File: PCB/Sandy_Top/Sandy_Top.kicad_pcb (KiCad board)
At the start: 2 copper layers, 285 x 75.1 mm, 31 parts, among them J2 Conn_02x02_Top_Bottom, J3 Conn_02x02_Top_Bottom

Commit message: 基板外形をLP版に変更。不要ファイル削除。
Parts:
- removed the SW_'1 at (186.6, 65.1)
- REF**: footprint locallib:60_Outline-Sandy-DN0040-Top-sw-hole -> locallib:SandyLP_outline_Top
- moved D17 11.0 mm to (142.5, 44.1), turned to -90 degrees
- moved D19 11.0 mm to (180.6, 44.1), turned to -90 degrees
- moved D16 10.6 mm to (123.5, 44.9), turned to -90 degrees
- moved D18 10.6 mm to (161.6, 44.9), turned to -90 degrees
- moved D15 10.3 mm to (142.5, 64.6), turned to -90 degrees
- moved D20 10.3 mm to (161.6, 64.6), turned to -90 degrees
- moved H10 3.57 mm to (173.5, 55.6)
- moved H9 1.19 mm to (142.5, 55.6)
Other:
- board size 285 x 75.1 mm -> 74.9 x 37 mm

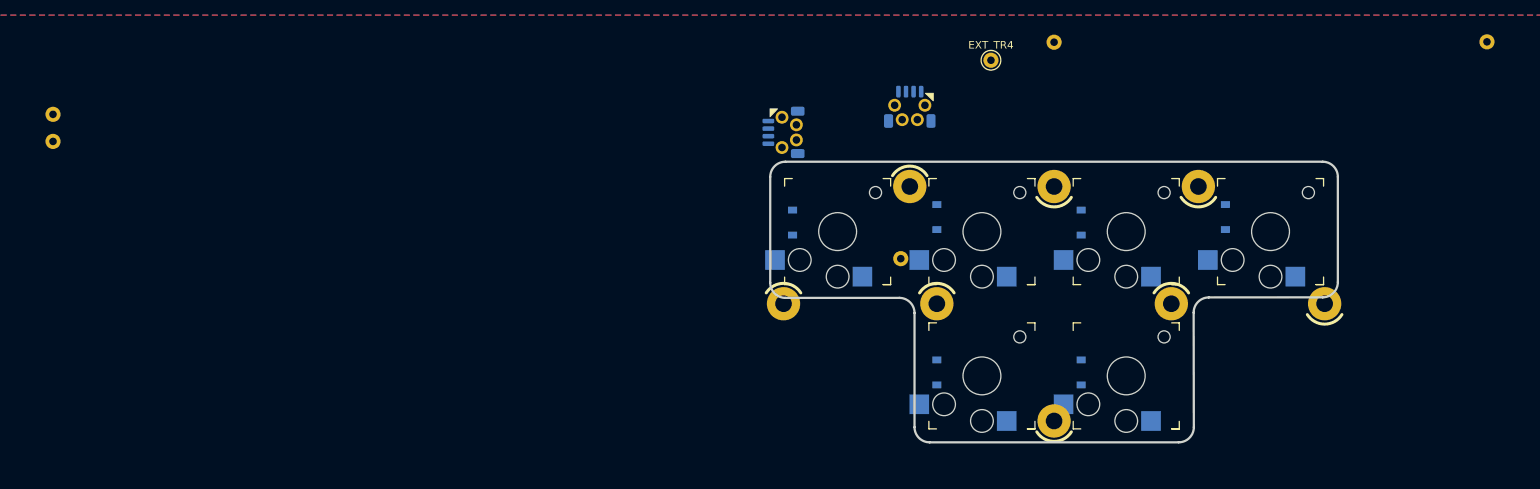
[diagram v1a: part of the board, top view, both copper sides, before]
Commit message: Topを仮配線。Midとの接続も一応確定
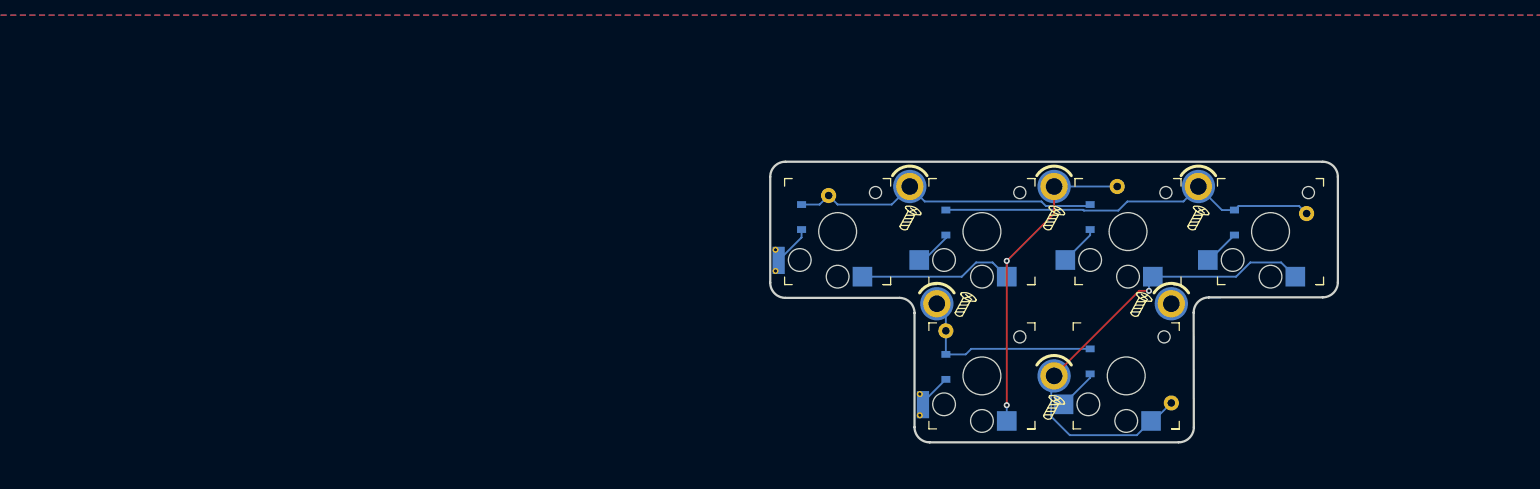
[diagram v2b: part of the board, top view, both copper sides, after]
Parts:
- removed EXT_TR5: Conn_01x01, locallib:TestPoint_THTPad_D2.0mm_Drill1.0mm
- removed the H6 at (177.0, 40.1)
- removed H8: MountingHole, locallib:MountingHole_2.2mm_M2_Pad_minimal
- removed J2, J3: Conn_02x02_Top_Bottom, locallib:JST_SH_SM04B-SRSS-TB_1x04-1MP_P1.00mm_Horizontal_wCable_housing_spare_pin_courtyard
- added REF**: ICON_Screw_Medium, locallib:ICON_Screw_Medium, F.Cu at (157.9, 71.8)
- added REF**: ICON_Screw_Medium, locallib:ICON_Screw_Medium, F.Cu at (169.4, 58.3)
- added REF**: ICON_Screw_Medium, locallib:ICON_Screw_Medium, F.Cu at (138.9, 46.8)
- added REF**: ICON_Screw_Medium, locallib:ICON_Screw_Medium, F.Cu at (157.9, 46.8)
- added REF**: ICON_Screw_Medium, locallib:ICON_Screw_Medium, F.Cu at (176.9, 46.8)
- added REF**: ICON_Screw_Medium, locallib:ICON_Screw_Medium, F.Cu at (146.2, 58.3)
- EXT_TR4: moved to B.Cu
- H1: renamed from H2; footprint locallib:MountingHole_2.2mm_M2_Pad_minimal -> locallib:MountingHole_1.8-2.2mm_M2_Pad_minimal
- H2: renamed from H3; footprint locallib:MountingHole_2.2mm_M2_Pad_minimal -> locallib:MountingHole_1.8-2.2mm_M2_Pad_minimal
- H3: renamed from H11; footprint locallib:MountingHole_2.2mm_M2_Pad_minimal -> locallib:MountingHole_1.8-2.2mm_M2_Pad_minimal
- H4: renamed from H12; footprint locallib:MountingHole_2.2mm_M2_Pad_minimal -> locallib:MountingHole_1.8-2.2mm_M2_Pad_minimal
- H5: renamed from H9; footprint locallib:MountingHole_2.2mm_M2_Pad_minimal -> locallib:MountingHole_1.8-2.2mm_M2_Pad_minimal
- H6: renamed from H10; footprint locallib:MountingHole_2.2mm_M2_Pad_minimal -> locallib:MountingHole_1.8-2.2mm_M2_Pad_minimal
- SW_;1, SW_[1: footprint locallib:Kailh_socket_ChocV2 -> locallib:Kailh_socket_ChocV2_small_#2pad
- moved EXT_TR0 103.0 mm to (128.2, 41.3)
- moved EXT_TC4 63.3 mm to (173.5, 68.7)
- moved D4 58.3 mm to (181.8, 44.9)
- moved SW_T1 57.2 mm to (186.6, 46.1)
- moved H3 56.9 mm to (177.0, 40.1)
- moved EXT_TR4 46.3 mm to (191.3, 43.7), turned to 180 degrees
- moved H2 38.9 mm to (158.0, 40.1), turned to 0 degrees
- moved H5 31.0 mm to (173.5, 55.6)
- moved EXT_TC3 20.8 mm to (166.3, 40.1)
- moved H1 19.1 mm to (138.9, 40.1), turned to 0 degrees
- moved SW_[1 19.1 mm to (129.4, 46.1)
- moved SW_]1 19.1 mm to (148.5, 46.1)
- moved SW_Y1 18.8 mm to (167.7, 46.1)
- moved H6 18.2 mm to (158.0, 65.1)
- moved D1 17.9 mm to (124.6, 44.1)
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- renumbered D17 to D1, D18 to D2, D19 to D3, D16 to D4, D15 to D5, D20 to D6
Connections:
- D6 pad 1: Top_row5 -> Top_row1
- H1 pad 1: Top_col3 -> Top_row0
- H2 pad 1: Top_col4 -> Top_col3
- H3 pad 1: Top_row0 -> Top_row4
- H5 pad 1: Top_row4 -> GND
- H6 pad 1: GND -> Top_col4
- SW_'1 pad 1: Top_col3 -> Top_col4
- SW_T1 pad 1: Top_col2 -> Top_col4
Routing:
- net Top_col3: track 0.00 -> 64.6 mm, vias 0 -> 2
- net Top_col4: track 0.00 -> 63.8 mm, vias 0 -> 1
- net Top_row4: track 0.00 -> 50.9 mm
- net Top_row0: track 0.00 -> 41.2 mm
- net Top_row1: track 0.00 -> 26.5 mm
- net Net-(D6-A): track 0.00 -> 5.48 mm
- net Net-(D3-A): track 0.00 -> 5.38 mm
- net Net-(D1-A): track 0.00 -> 5.32 mm
- net Net-(D2-A): track 0.00 -> 5.11 mm
- net Net-(D4-A): track 0.00 -> 4.88 mm
- net Net-(D5-A): track 0.00 -> 4.88 mm
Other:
- board text added: "#SandyLP_kbd DN0010 Top by @jpskenn"
- board text removed: "#Sandy_kbd DN0040, Top & Plate for Mid by @jpskenn"
- board text removed: "Top 1"
- board text removed: "Top 2"
- board text removed: "Top 3"
- board text removed: "to Base"
- board text removed: "to Mid"
